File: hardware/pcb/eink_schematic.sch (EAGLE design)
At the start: 13 parts, among them J1 AA_BAT_PACKSMD, J2 5.5x2.1mm Barrel, Q1 FDN340P, U1 NUCLEUM, U2 LTC3531ES6-3PBF, U4 MAX6326UR29+

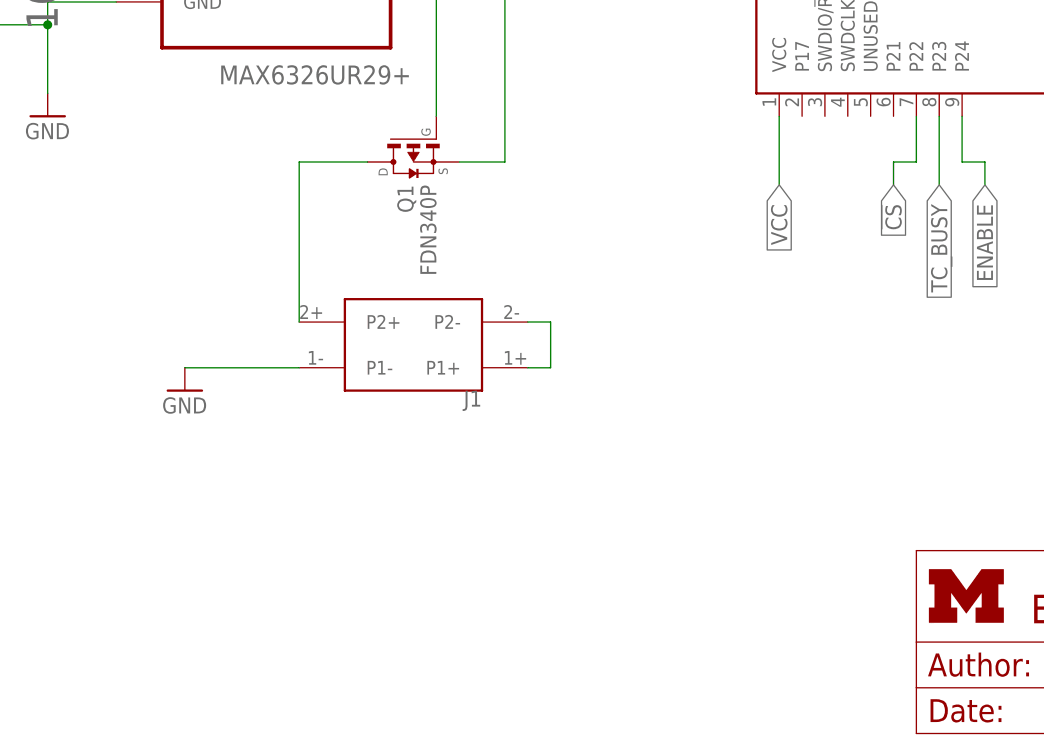
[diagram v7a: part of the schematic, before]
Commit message: re-wired and created eagle part for through-hole battery pack
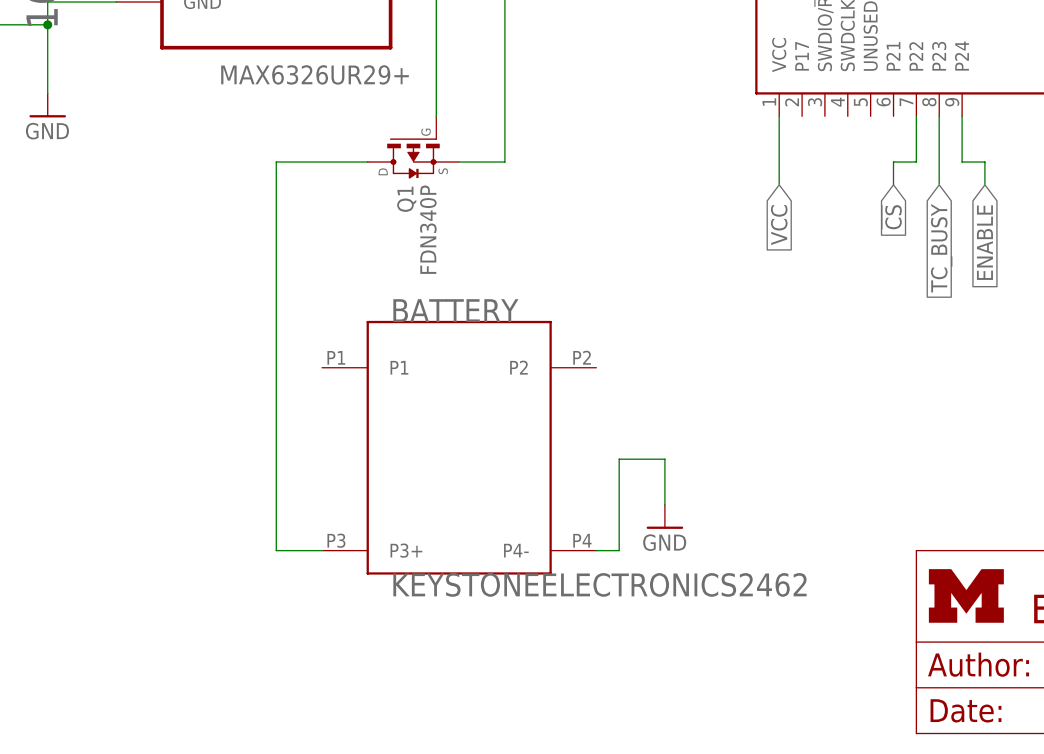
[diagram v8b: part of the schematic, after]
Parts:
- removed J1: AA_BAT_PACKSMD, connector:AA_BAT_PACKSMD
- added BATTERY: KEYSTONEELECTRONICS2462, through_hole_battery_pack:KEYSTONEELECTRONICS2462
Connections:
- removed net N$5: J1.P1+, J1.P2-
- net GND: now also BATTERY.P4-; no longer J1.P1-
- net N$4: now also BATTERY.P3+; no longer J1.P2+
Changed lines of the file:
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@@
 <attribute name="DIGIKEY" value="490-10693-1-ND"/>
-</part>
-<part name="J1" library="connector" deviceset="AA_BAT_PACK" device="SMD">
-<attribute name="DIGIKEY" value="36-1012-ND"/>
 </part>
 <part name="GND2" library="umich" deviceset="GND" device=""/>
@@
 </part>
 <part name="R4" library="Yageo_By_element14_Batch_1" deviceset="RC0603JR-07100KL" device="" value="100K Ohms"/>
+<part name="BATTERY" library="through_hole_battery_pack" deviceset="KEYSTONEELECTRONICS2462" device="">
+<attribute name="DIGIKEY" value="36-2462-ND"/>
+</part>
 </parts>
 <sheets>
@@
 <attribute name="DIGIKEY" x="106.68" y="147.32" size="1.778" layer="96" display="off"/>
 </instance>
-<instance part="J1" gate="G$1" x="91.44" y="43.18" rot="R90">
-<attribute name="DIGIKEY" x="91.44" y="43.18" size="1.778" layer="96" rot="R90" display="off"/>
-</instance>
 <instance part="GND2" gate="1" x="106.68" y="124.46"/>
-<instance part="GND3" gate="1" x="66.04" y="38.1"/>
+<instance part="GND3" gate="1" x="119.38" y="22.86"/>
 <instance part="D1" gate="G$1" x="76.2" y="104.14">
 <attribute name="DIGIKEY" x="76.2" y="104.14" size="1.778" layer="96" display="off"/>
@@
 </instance>
 <instance part="R4" gate="A" x="43.18" y="81.28" rot="R90"/>
+<instance part="BATTERY" gate="KE2462" x="86.36" y="17.78">
+<attribute name="DIGIKEY" x="86.36" y="17.78" size="1.778" layer="96" display="off"/>
+</instance>
 </instances>
 <busses>
@@
 </segment>
 <segment>
-<pinref part="J1" gate="G$1" pin="P1-"/>
+<pinref part="BATTERY" gate="KE2462" pin="P4-"/>
+<wire x1="111.76" y1="20.32" x2="114.3" y2="20.32" width="0.1524" layer="91"/>
+<wire x1="114.3" y1="20.32" x2="114.3" y2="30.48" width="0.1524" layer="91"/>
 <pinref part="GND3" gate="1" pin="GND"/>
-<wire x1="78.74" y1="40.64" x2="66.04" y2="40.64" width="0.1524" layer="91"/>
+<wire x1="114.3" y1="30.48" x2="119.38" y2="30.48" width="0.1524" layer="91"/>
+<wire x1="119.38" y1="30.48" x2="119.38" y2="25.4" width="0.1524" layer="91"/>
 </segment>
 </net>
@@
 <net name="N$4" class="0">
 <segment>
-<pinref part="J1" gate="G$1" pin="P2+"/>
-<wire x1="78.74" y1="45.72" x2="78.74" y2="63.5" width="0.1524" layer="91"/>
 <pinref part="Q1" gate="G$1" pin="D"/>
-<wire x1="78.74" y1="63.5" x2="86.36" y2="63.5" width="0.1524" layer="91"/>
-</segment>
-</net>
-<net name="N$5" class="0">
-<segment>
-<pinref part="J1" gate="G$1" pin="P2-"/>
-<wire x1="104.14" y1="45.72" x2="106.68" y2="45.72" width="0.1524" layer="91"/>
-<wire x1="106.68" y1="45.72" x2="106.68" y2="40.64" width="0.1524" layer="91"/>
-<pinref part="J1" gate="G$1" pin="P1+"/>
-<wire x1="106.68" y1="40.64" x2="104.14" y2="40.64" width="0.1524" layer="91"/>
-</segment>
-</net>
+<wire x1="86.36" y1="63.5" x2="76.2" y2="63.5" width="0.1524" layer="91"/>
+<wire x1="76.2" y1="63.5" x2="76.2" y2="20.32" width="0.1524" layer="91"/>
+<pinref part="BATTERY" gate="KE2462" pin="P3+"/>
+<wire x1="76.2" y1="20.32" x2="81.28" y2="20.32" width="0.1524" layer="91"/>
+</segment>
+</net>
